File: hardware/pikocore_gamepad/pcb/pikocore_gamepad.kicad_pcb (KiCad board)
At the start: 4 copper layers, 120 x 80 mm, 63 parts, among them J1 PHONES, J4 ST7789_240x240, J5 SPEAKER 8R, SW10 BTN_R, SW11 BTN_START, SW12 BTN_SELECT, SW13 NAV5, SW15 PWR, SW5 BTN_X, SW6 BTN_Y, SW7 BTN_A, SW8 BTN_B, SW9 BTN_L, U1 RP2350-Plus-16MB, U2 TPS61023DRLR, U3 PT2308-S, U4 PAM8302A, U5 PCM5102APWR

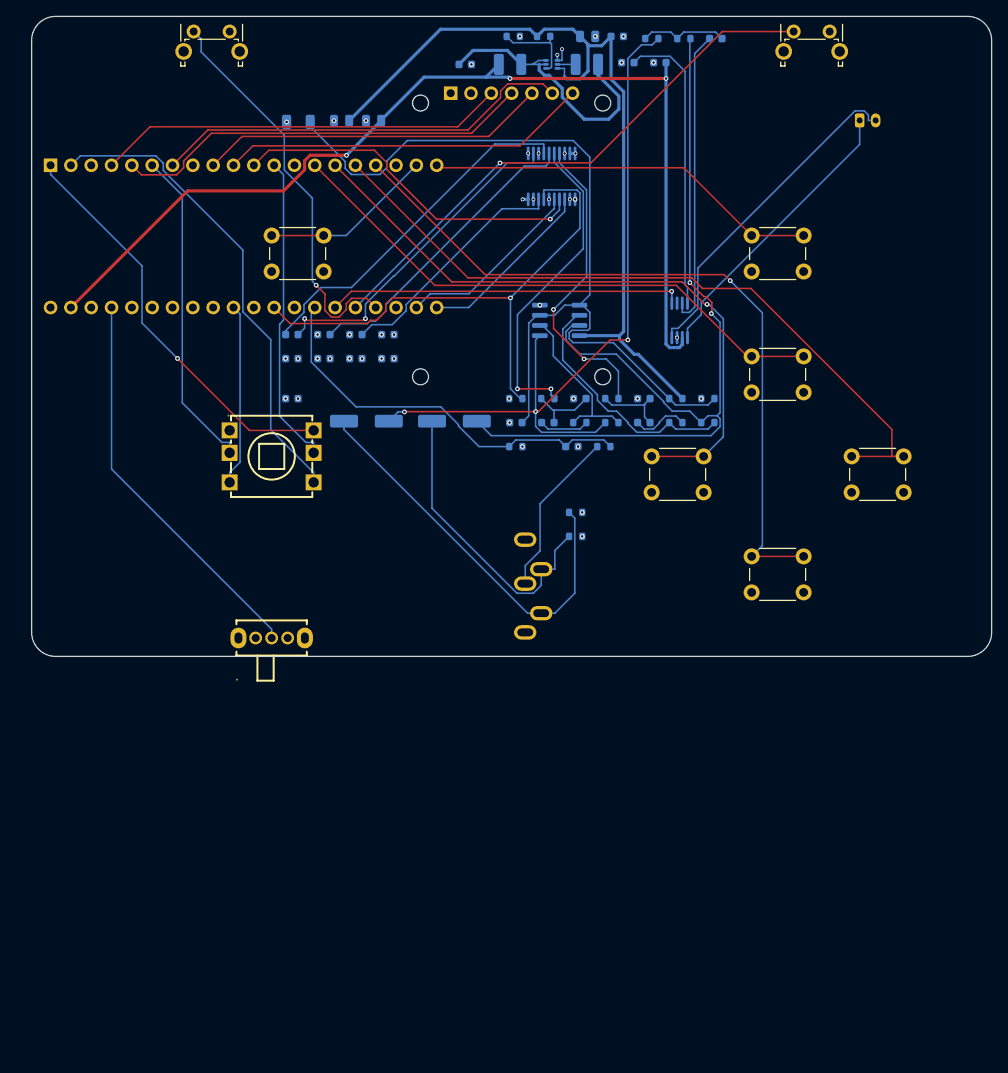
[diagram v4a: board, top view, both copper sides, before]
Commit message: hw: placa reducida a 100x80 mm, re-ruteada y con todas las puertas en verde
Los dos grupos de controles fijaban el ancho y sobraban ~30mm de aire. El
rombo X/Y/A/B pasa a cuerpo en X=70 (espejo del NAV5 en X=30 respecto del
centro), Select al mismo eje, el gatillo R a x=75.25 (simetrico de L) y J5
a (91, 13). El lazo del boost corre 5mm a la izquierda para alejarse de los
anclajes NPTH del gatillo y U3 baja a (58, 35) para no quedar a 0.8mm de
los pines pasantes de X. FREE_REGIONS recalculadas; template DXF de Rhino
regenerado a 100x80 (el _MOD.dxf sigue siendo el de 120).

manual_tracks.py deja de usar coordenadas absolutas: las pistas de U2 y
los puentes de los seis tacts se derivan de placements.py.

Re-ruteada con freerouting 2.4.1 (jar del plugin de KiCad 10, Java 25):
534 pistas, 98 vias. Tres bugs de KiCad 9.0.1 rodeados en el pipeline:
- Footprint.Flip() deja los pads PTH sin capas internas y el plano no les
  da radio termico (10 conexiones abiertas): reparar_capas_pth() en
  gen_pcb.py, tambien desde finish_pcb.py.
- PCB_VIA.SetWidth(int) abre un assert modal y cuelga el script: se pasa
  PADSTACK.ALL_LAYERS en manual_tracks.py y plane_vias.py.
- El (image ...) del DSN lleva prefijo de libreria desde que el FPID lo
  tiene: route_io.py acepta las dos formas al quitar el outline del SOT-563.

Puertas: 201 tests, G-0/G-5/G-4/G-2/placement OK, ERC 0 errores, DRC 0
errores / 0 abiertas / 0 paridad (10 avisos: serigrafia al borde, NPTH de
SW9/SW10), G-F al dia, fab con las 4 capas (16 archivos). Docs y skill
pcb-verify actualizadas con el estado y las trampas de 9.0.1.

Co-Authored-By: Claude Fable 5.1 <noreply@anthropic.com>
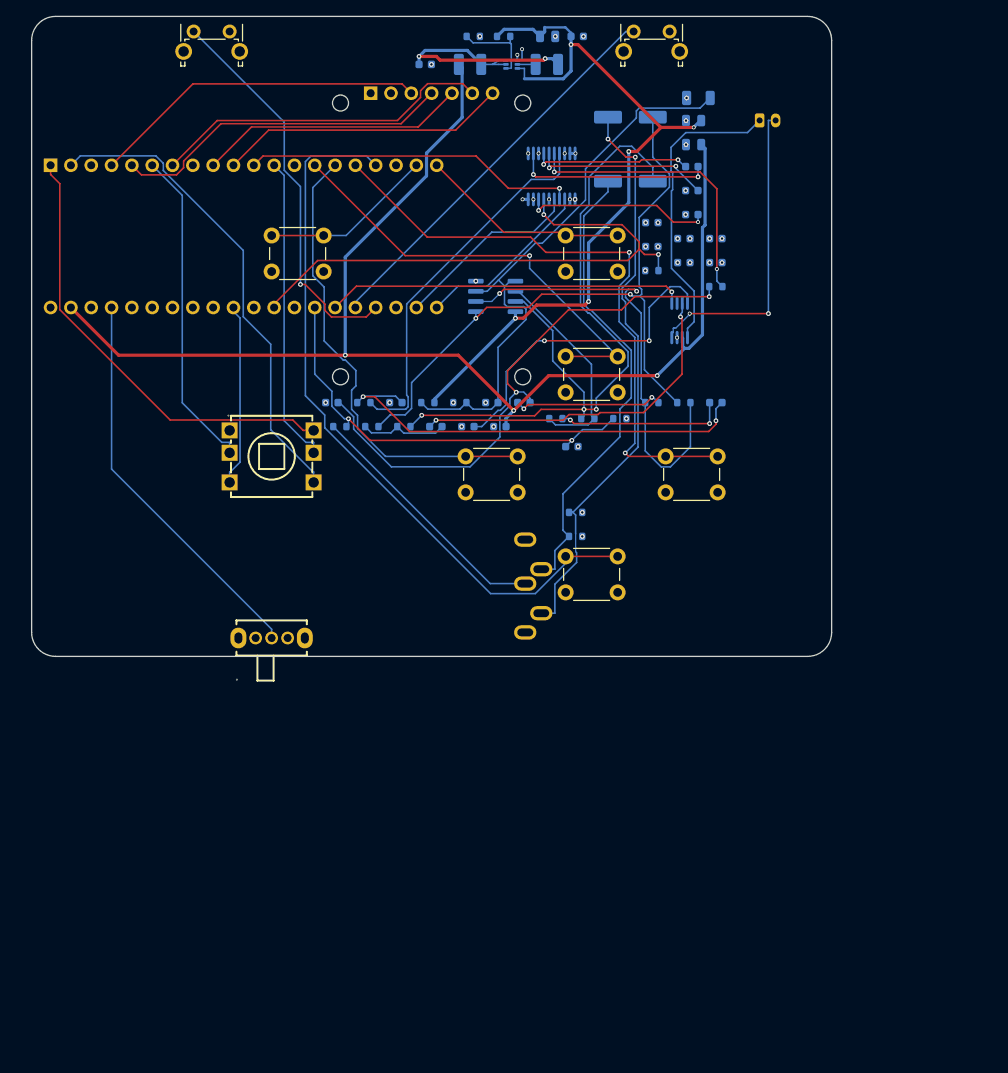
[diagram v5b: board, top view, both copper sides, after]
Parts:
- moved C25 59.8 mm to (50.5, 51.3)
- moved R16 59.8 mm to (42.5, 51.3)
- moved R17 59.8 mm to (46.5, 51.3)
- moved C16 55.7 mm to (85.5, 30.8)
- moved C8 54.2 mm to (82.5, 18.8)
- moved C12 51.2 mm to (81.5, 27.8)
- moved C13 51.2 mm to (85.5, 27.8)
- moved C23 50.3 mm to (74.8, 12.6)
- moved C19 50.1 mm to (83.3, 10.2)
- moved C26 49.7 mm to (54.5, 51.3)
- moved C27 49.7 mm to (58.5, 51.3)
- moved C9 49.4 mm to (82.5, 21.8)
- moved C10 44.6 mm to (82.5, 24.8)
- moved C6 44.0 mm to (82.7, 13.0)
- moved C28 40.1 mm to (82.7, 16.0)
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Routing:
- net AOUT_L: track 8.35 -> 68.5 mm, vias 0 -> 2
- net AOUT_R: track 8.81 -> 55.6 mm, vias 0 -> 2
- net OPL_N: track 20.6 -> 56.4 mm, vias 0 -> 2
- net VREF25: track 109.8 -> 74.1 mm
- net VSYS: track 127.8 -> 158.7 mm
- net CAPM: track 44.2 -> 19.7 mm, vias 0 -> 2
- net BTN_SELECT: track 49.5 -> 26.3 mm
- net BTN_Y: track 81.2 -> 58.4 mm, vias 1 -> 0
- net JACK_L: track 50.8 -> 72.5 mm, vias 0 -> 2
- net JACK_R: track 37.9 -> 58.6 mm
- net AUDIO_R: track 108.9 -> 89.2 mm, vias 2 -> 3
- net BTN_R: track 69.1 -> 49.5 mm, vias 1 -> 0
- net CAPP: track 41.4 -> 24.6 mm
- net VNEG: track 37.9 -> 21.9 mm, vias 0 -> 2
- net BTN_X: track 71.0 -> 55.2 mm, vias 0 -> 1
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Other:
- board size 120 x 80 mm -> 100 x 80 mm

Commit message: hw: D-pad de cuatro tacts 6x6 en lugar del NAV5, re-ruteo determinista del boost
El NAV5 de 5 vias es un solo actuador y no deja pulsar dos direcciones a la
vez, que es lo que piden Up+Down+B+A (reset de FX) y Down+Left+X+B (clock
lock). Vuelven SW1-SW4 (SW_PUSH_6mm) en cruz de 12.5mm centrada en X=30,
espejo del rombo; BTN_OK desaparece y GP26 queda libre con GP27/28; Start
pasa a x=26.75 para centrar su cuerpo en X=30. manual_tracks.py toma la lista
de tacts de netlist.TACTS, sin tercera copia. Tests, stub de firmware y doc
de pinout actualizados (196 tests).

Ruteo: freerouting 2.4.1 se lanza con -Djava.awt.headless=true -mt 1. Con
ventana, un NullPointerException en el repintado de AWT interrumpe el fanout
y el .ses sale con 60+ nets abiertas y exit 0. Las pistas manuales solo a
0/45/90 grados: con otro angulo la normalizacion oscila y aborta. Todo el
lazo del boost va ahora a mano y relativo a U2 (U2_5V hasta C5.1, C7_5V,
L1_VSYS_F, C4_VSYS_F): freerouting cerraba esos tramos una corrida si y
otra no. NPTH_KEEPOUT sube de 0.60 a 0.75 (BTN_R quedaba a 0.36mm del
anclaje de SW10).

Puertas: G-0/G-5/G-4/G-2/placement OK, ERC 0 errores (3 avisos GP26/27/28
reservados), DRC 0 errores / 0 abiertas / 0 paridad, G-F al dia, fab con las
4 capas (38 lineas de BOM, 17 sin LCSC: THT manuales y los 470uF).

Co-Authored-By: Claude Fable 5.1 <noreply@anthropic.com>
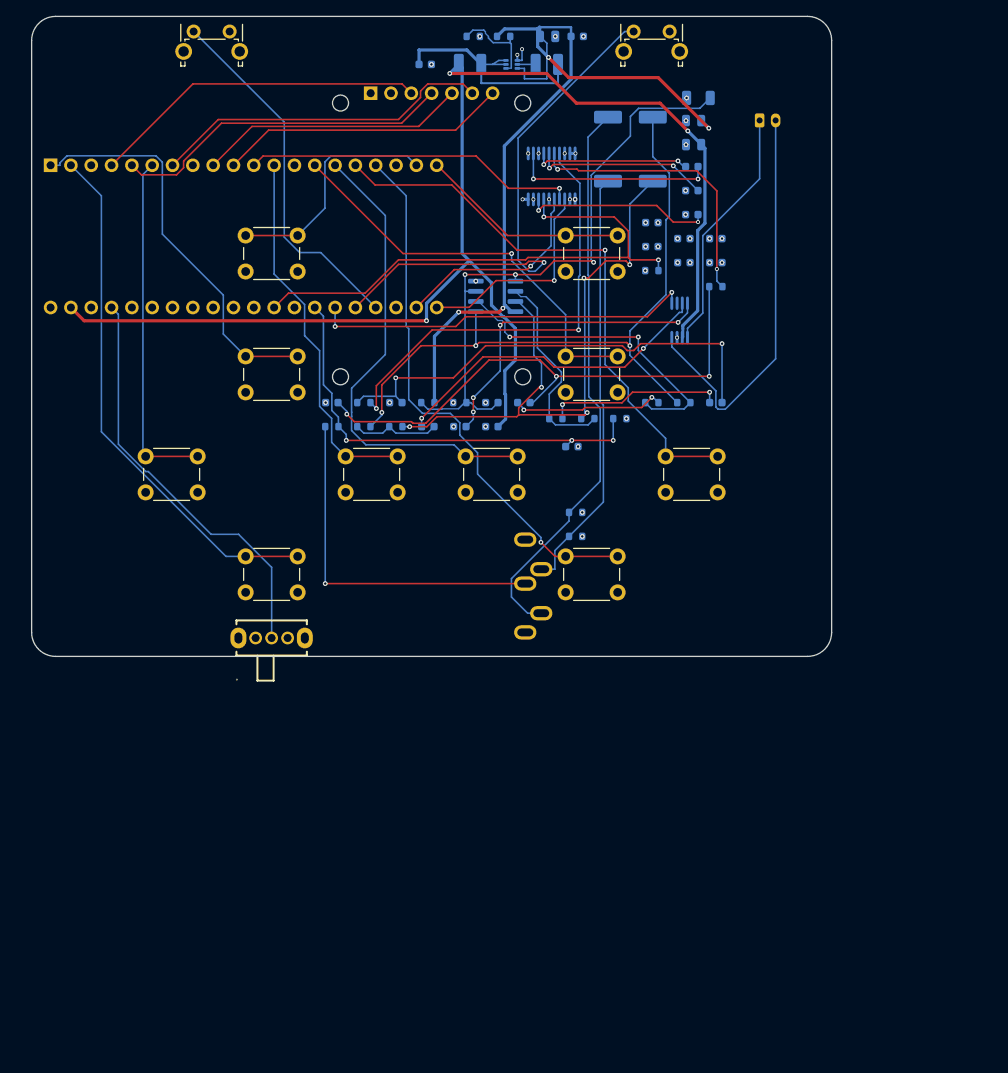
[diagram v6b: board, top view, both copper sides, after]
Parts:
- removed SW13: NAV5, gamesetup_lcsc:SW-TH_WS-1004-ARL10026
- added SW1: DPAD_UP, Button_Switch_THT:SW_PUSH_6mm, F.Cu at (26.8, 42.5)
- added SW2: DPAD_DOWN, Button_Switch_THT:SW_PUSH_6mm, F.Cu at (26.8, 67.5)
- added SW3: DPAD_LEFT, Button_Switch_THT:SW_PUSH_6mm, F.Cu at (14.2, 55.0)
- added SW4: DPAD_RIGHT, Button_Switch_THT:SW_PUSH_6mm, F.Cu at (39.2, 55.0)
- moved SW11 3.25 mm to (26.8, 27.4)
- moved C25 1.00 mm to (49.5, 51.3)
- moved C26 1.00 mm to (53.5, 51.3)
- moved C27 1.00 mm to (57.5, 51.3)
- moved R16 1.00 mm to (41.5, 51.3)
- moved R17 1.00 mm to (45.5, 51.3)
- moved R18 1.00 mm to (37.5, 51.3)
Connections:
- U1 pad 31: BTN_OK -> EXP_GP26
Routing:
- net BTN_B: track 91.5 -> 68.0 mm, vias 0 -> 1
- net BTN_OK: track 22.8 -> 0.00 mm
- net OPL_N: track 56.4 -> 40.0 mm
- net BTN_R: track 49.5 -> 65.5 mm, vias 0 -> 1
- net 5V: track 96.8 -> 109.3 mm, vias 5 -> 4
- net JACK_DETSW: track 32.1 -> 44.6 mm, vias 0 -> 1
- net SPK_N: track 39.1 -> 51.0 mm, vias 2 -> 0
- net AUDIO_R: track 89.2 -> 77.5 mm, vias 3 -> 5
- net DACOUT_R: track 46.5 -> 55.2 mm, vias 0 -> 2
- net DPAD_RIGHT: track 38.6 -> 46.6 mm
- net BTN_START: track 21.7 -> 29.3 mm
- net VSYS: track 158.7 -> 166.3 mm
- net SPK_P: track 37.9 -> 30.9 mm
- net DPAD_UP: track 56.5 -> 50.0 mm
- net BTN_A: track 77.4 -> 71.0 mm, vias 2 -> 1
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
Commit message: hw: pantalla por flex (DM-TFT13-377 24P + FPC 0.5mm) y layout del estudio ergonomico
El modulo LCD de 7 pines pasantes se reemplaza por el panel desnudo
DisplayModule DM-TFT13-377 variante 24 pines (LH133T-IF05, ST7789VW,
datasheet en hardware/pikocore_gamepad/datasheets/) pegado al frente, con
el FPC de 0.5mm al conector J4 XUNPU FPC-05FB-24PH20 (LCSC C2856831, huella
y STEP importados con easyeda2kicad). LCSC no tiene paneles de 1.3" en
stock y la variante de 12 pines usa FPC de 0.7mm, paso para el que LCSC no
vende conector. 4-SPI con IM=1, CS a masa (siempre seleccionado, como el
modulo), RD y DB0-7 a masa, TE a GP26 (LCD_TE). Backlight desde VSYS por
R21 (24R, perilla de brillo) y Q1 2N7002 (C8545) con R22 de pulldown;
C30/C31 de desacoplo. LCD1 es una huella sin pads generada por gen_fp.py
(origen = centro del area activa), DNP para el CPL pero en el BOM.

Layout segun el estudio ergonomico: panel con el BL a 3.0mm del borde
superior (area activa y 4.6-28), D-pad y rombo centrados en y 53.2 con paso
12.5, Select (50, 51) y Start (50, 63) apilados en la columna central, J4 en
(50, 44.6) rot 180 justo donde caen los contactos del flex desplegado,
R19/R20 bajados a y 72.5/75.5 por los pines de B. Los pulgares quedan 8mm
por debajo del vidrio; Up/X al costado de la franja sin vidrio.

G-0 queda ROJO a proposito: LCD_FPC_PIN_ORDER (V-8) no sale del datasheet
(lado de los contactos del FPC); se mide con el panel en mano y, si esta
espejado, J4 va a rot 0. gen_fab.py solo genera con --force hasta entonces.

Pipeline: plane_vias.py saltea el pad si hay una via propia a <0.6mm (los
13 GND del conector a 0.5mm daban hole_to_hole) y el fanout rechaza
candidatos pegados a una via de la misma net; finish_pcb.py borra stubs
colgantes. Tests reescritos para el panel (181). Puertas: G-5/G-4/G-2/
placement OK, 245 conexiones identicas, ERC 0 errores (2 avisos GP27/28),
DRC 0 errores / 0 abiertas / 0 paridad (10 avisos conocidos).

Co-Authored-By: Claude Fable 5.1 <noreply@anth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
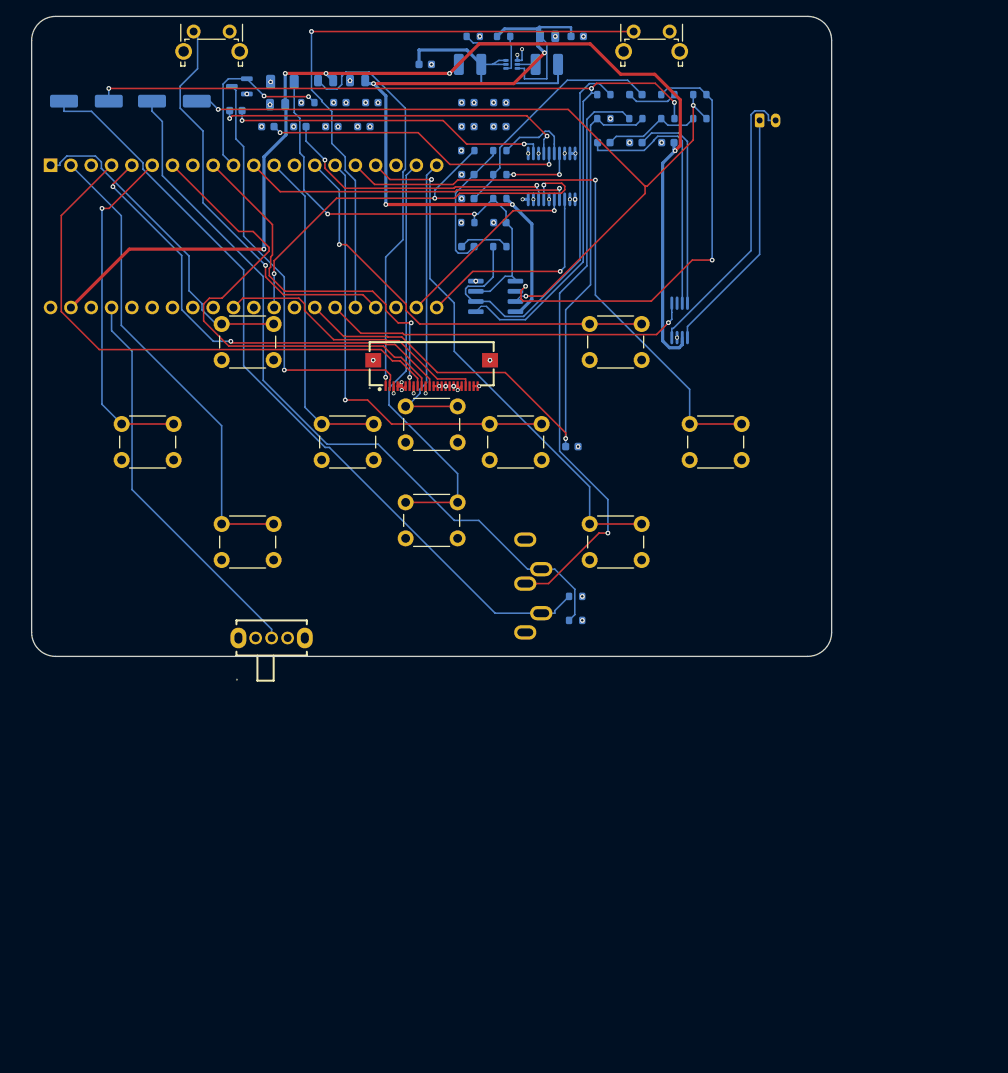
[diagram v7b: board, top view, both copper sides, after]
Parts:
- added C30: 1uF, Capacitor_SMD:C_0603_1608Metric, B.Cu at (38.5, 10.8)
- added C31: 100nF, Capacitor_SMD:C_0603_1608Metric, B.Cu at (42.5, 10.8)
- added LCD1: DM-TFT13-377-24P, gamesetup_fp:LCD_LH133T_24P, F.Cu at (50.0, 16.3)
- added Q1: 2N7002, Package_TO_SOT_SMD:SOT-23, B.Cu at (26.0, 8.74)
- added R21: 24R, Capacitor_SMD:C_0805_2012Metric, B.Cu at (36.7, 8.03)
- added R22: 100k, Resistor_SMD:R_0603_1608Metric, B.Cu at (34.5, 10.8)
- J4: value ST7789_240x240 -> LCD_FPC; footprint gamesetup_fp:LCD_ST7789_240x240_7P -> gamesetup_lcsc:FPC-SMD_24P-P0.50_FPC-05FB-24PH20
- moved C23 68.0 mm to (6.84, 10.6)
- moved C24 57.9 mm to (17.8, 10.6)
- moved C8 57.4 mm to (25.5, 11.8)
- moved R16 54.1 mm to (79.5, 12.8)
- moved R17 54.1 mm to (83.5, 12.8)
- moved R18 54.1 mm to (75.5, 12.8)
- moved C9 53.6 mm to (29.5, 13.8)
- moved C28 52.2 mm to (30.7, 11.0)
- moved C19 52.0 mm to (31.3, 8.20)
- moved C10 50.2 mm to (33.5, 13.8)
- moved R13 42.9 mm to (79.5, 9.78)
- moved R14 42.9 mm to (83.5, 9.78)
- moved C12 42.4 mm to (41.5, 13.8)
- moved C6 42.3 mm to (40.7, 8.03)
- moved C25 41.8 mm to (71.5, 15.8)
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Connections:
- J4 pad 1: GND -> BL_A
- J4 pad 2: 3V3 -> BL_K
- J4 pad 3: LCD_SCK -> GND
- J4 pad 4: LCD_MOSI -> 3V3
- J4 pad 5: LCD_RES -> 3V3
- J4 pad 6: LCD_DC -> 3V3
- J4 pad 7: LCD_BLK -> LCD_RES
- U1 pad 31: EXP_GP26 -> LCD_TE
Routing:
- net BL_K: track 0.00 -> 53.1 mm, vias 0 -> 1
- net AOUT_L: track 67.9 -> 17.2 mm, vias 3 -> 0
- net BL_A: track 0.00 -> 50.5 mm, vias 0 -> 1
- net DACOUT_R: track 55.2 -> 9.28 mm
- net JACK_R: track 53.3 -> 94.6 mm
- net LCD_TE: track 0.00 -> 35.1 mm
- net JACK_DET: track 55.4 -> 87.5 mm, vias 3 -> 1
- net AUDIO_L: track 84.5 -> 115.9 mm
- net OPR_N: track 25.6 -> 56.8 mm, vias 0 -> 2
- net JACK_DETSW: track 44.6 -> 74.6 mm
- net AOUT_R: track 59.0 -> 29.7 mm, vias 2 -> 0
- net JACK_L: track 70.8 -> 99.0 mm
- net LCD_SCK: track 42.2 -> 69.9 mm
- net DACOUT_L: track 35.5 -> 9.37 mm, vias 2 -> 0
- net CAPM: track 19.6 -> 44.2 mm
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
